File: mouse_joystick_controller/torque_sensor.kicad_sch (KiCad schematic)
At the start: 1 part

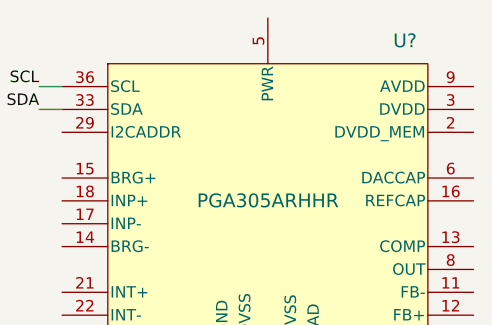
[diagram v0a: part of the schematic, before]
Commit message: Rearrange sheets
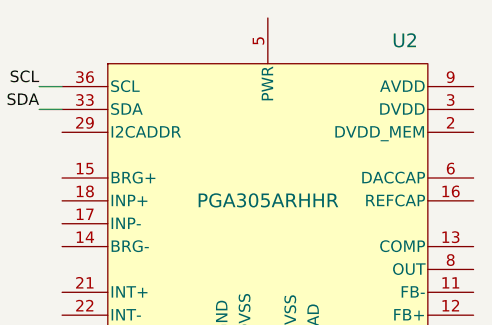
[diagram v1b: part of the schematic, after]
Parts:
- gave numbers to parts that had none: 1
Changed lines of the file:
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@@
   (title_block
     (title "mouse_joystick_controller")
-    (date "2023-05-22")
+    (date "2023-05-24")
     (rev "2.0")
     (company "Howard Hughes Medical Institute")
@@
   (symbol (lib_id "Janelia:PGA305ARHHR") (at 143.51 88.9 0) (unit 1)
     (in_bom yes) (on_board yes) (dnp no)
-    (property "Reference" "U?" (at 158.75 71.12 0) (do_not_autoplace)
+    (property "Reference" "U2" (at 158.75 71.12 0) (do_not_autoplace)
       (effects (font (size 1.524 1.524)))
     )
@@
       (project "mouse_joystick_controller"
         (path "/cc457ebc-4af6-4663-b19f-8cb38f061cb4/b0ea6103-1b85-4f11-9b33-df89645fe9c7"
-          (reference "U?") (unit 1)
+          (reference "U2") (unit 1)
         )
       )

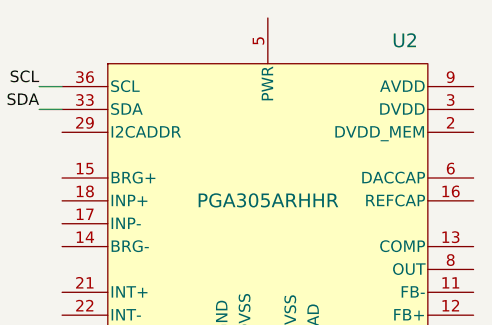
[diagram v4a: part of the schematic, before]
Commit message: Test pin rcpt
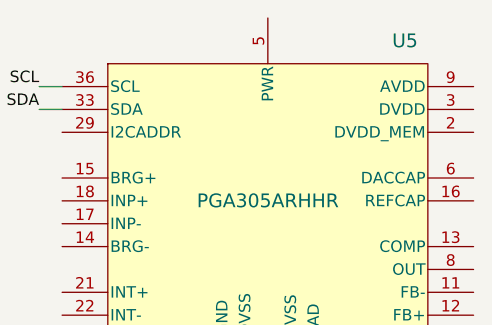
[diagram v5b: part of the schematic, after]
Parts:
- renumbered U2 to U5
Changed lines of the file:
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@@
   (title_block
     (title "mouse_joystick_controller")
-    (date "2023-06-07")
+    (date "2023-06-09")
     (rev "2.0")
     (company "Howard Hughes Medical Institute")
@@
   (symbol (lib_id "Janelia:PGA305ARHHR") (at 143.51 88.9 0) (unit 1)
     (in_bom yes) (on_board yes) (dnp no)
-    (property "Reference" "U2" (at 158.75 71.12 0) (do_not_autoplace)
+    (property "Reference" "U5" (at 158.75 71.12 0) (do_not_autoplace)
       (effects (font (size 1.524 1.524)))
     )
@@
       (effects (font (size 1.27 1.27)) hide)
     )
+    (property "Sim.Enable" "0" (at 143.51 88.9 0)
+      (effects (font (size 1.27 1.27)) hide)
+    )
     (pin "10")
     (pin "11")
@@
       (project "mouse_joystick_controller"
         (path "/cc457ebc-4af6-4663-b19f-8cb38f061cb4/b0ea6103-1b85-4f11-9b33-df89645fe9c7"
-          (reference "U2") (unit 1)
+          (reference "U5") (unit 1)
         )
       )
